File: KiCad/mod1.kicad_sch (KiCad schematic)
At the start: 67 parts, among them M1 Fan_4pin, M2 Fan_4pin, U1 W25Q128JVS

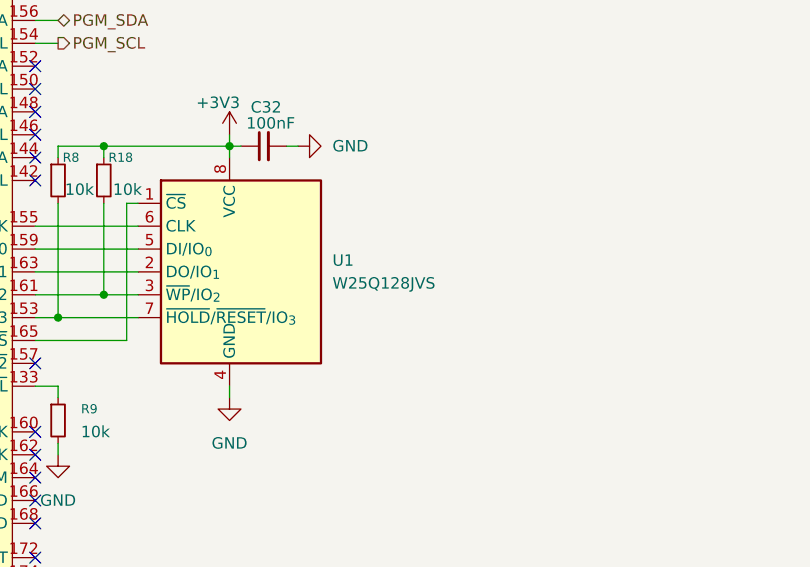
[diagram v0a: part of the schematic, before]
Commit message: Add TVS diodes for ESD protection
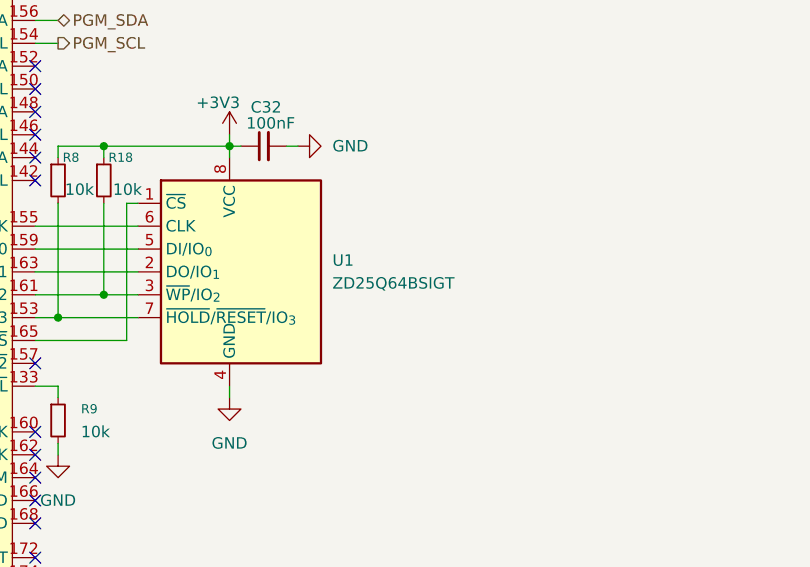
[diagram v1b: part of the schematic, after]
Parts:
- U1: value W25Q128JVS -> ZD25Q64BSIGT
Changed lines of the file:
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@@
 			)
 		)
-		(property "Value" "W25Q128JVS"
+		(property "Value" "ZD25Q64BSIGT"
 			(at 358.14 264.1599 0)
 			(effects

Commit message: Add more footprints
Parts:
- A1: footprint Module_LattePanda:LattePanda_Module_H8.0mm_Horizontal -> 124B-150A02:ATTEND_124B-150A02
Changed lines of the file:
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@@
 			)
 		)
-		(property "Footprint" "Module_LattePanda:LattePanda_Module_H8.0mm_Horizontal"
+		(property "Footprint" "124B-150A02:ATTEND_124B-150A02"
 			(at 284.48 199.39 0)
 			(effects

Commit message: Add more footprints
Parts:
- C1, C10, C11, C12, C13, C14, C15, C16, C17, C18, C19, C2, C20, C21, C22, C23, C24, C25, C26, C27, C28, C29, C3, C30, C31, C32, C33, C4, C5, C6, C7, C8, C9: footprint (none) -> Capacitor_SMD:C_0603_1608Metric
- D1: footprint (none) -> LED_SMD:LED_0805_2012Metric
- D3, D4: footprint (none) -> Diode_SMD:D_SOD-123
- M1, M2: footprint (none) -> Connector:FanPinHeader_1x04_P2.54mm_Vertical
- R1, R7: footprint (none) -> Resistor_SMD:R_0805_2012Metric
- R19, R23, R24: value 21.5k -> 22k; footprint (none) -> Resistor_SMD:R_0603_1608Metric
- R2, R20, R22, R25, R26, R3, R4, R5, R6: footprint (none) -> Resistor_SMD:R_0603_1608Metric

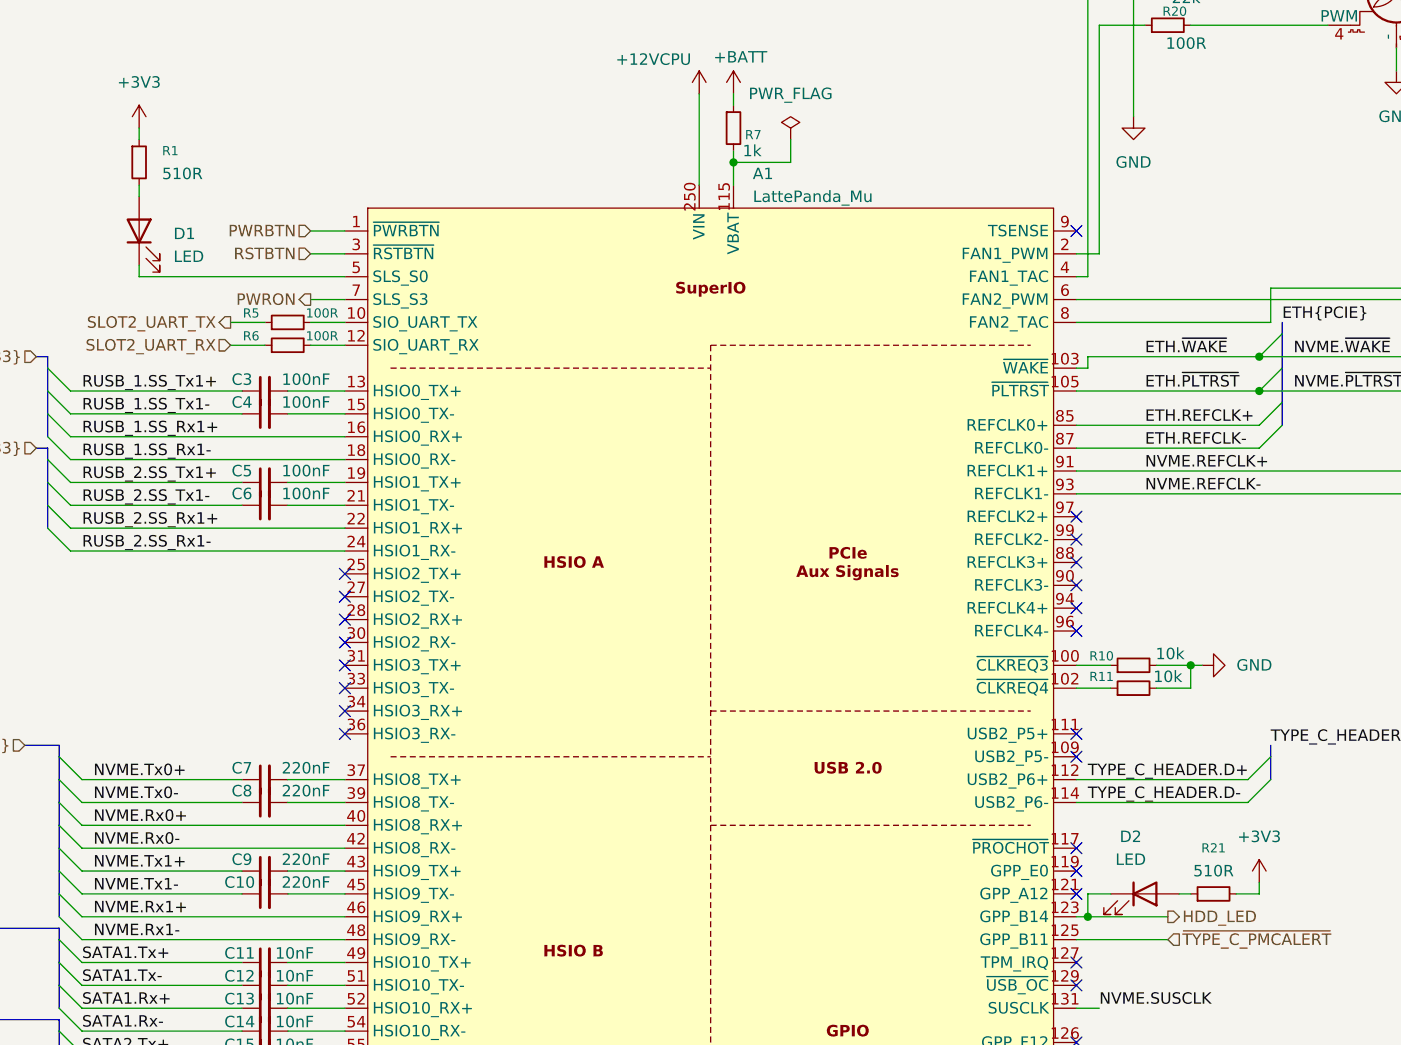
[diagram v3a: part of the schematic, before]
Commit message: Lots of tiny capacitors
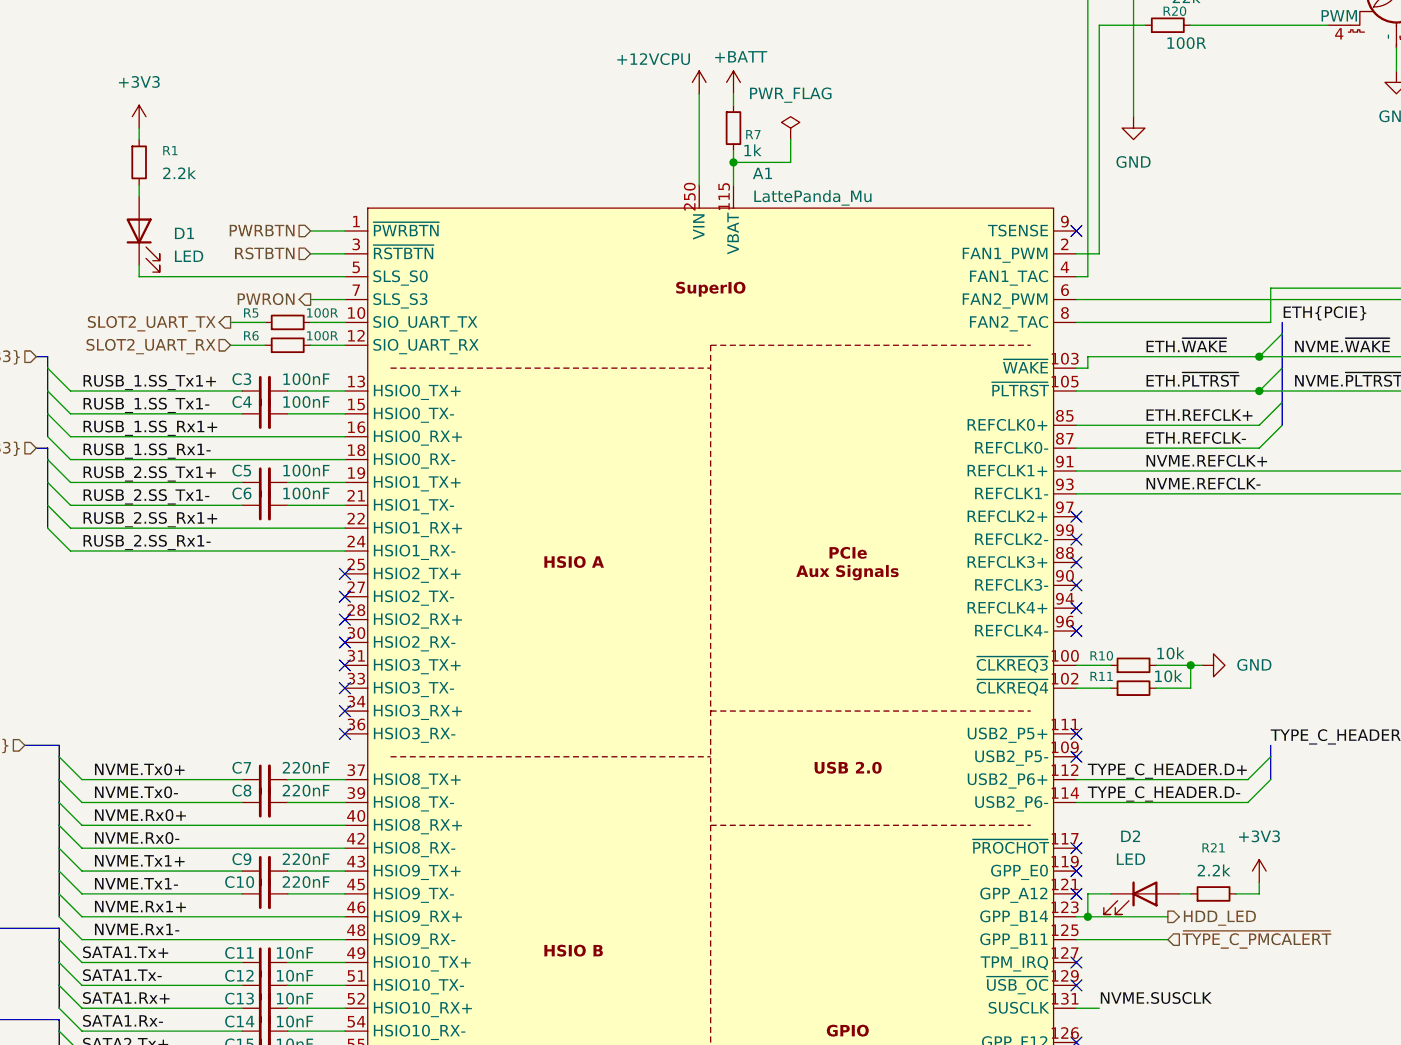
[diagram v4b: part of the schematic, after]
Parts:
- C1, C10, C11, C12, C13, C14, C15, C16, C17, C18, C19, C2, C20, C21, C22, C23, C24, C25, C26, C27, C28, C29, C3, C30, C31, C32, C33, C4, C5, C6, C7, C8, C9: footprint Capacitor_SMD:C_0603_1608Metric -> Capacitor_SMD:C_0402_1005Metric
- R1: value 510R -> 2.2k; footprint Resistor_SMD:R_0805_2012Metric -> Resistor_SMD:R_0402_1005Metric
- R10, R11, R12, R13, R14, R15, R16, R17, R18, R8: footprint (none) -> Resistor_SMD:R_0402_1005Metric
- R19, R2, R20, R22, R23, R24, R25, R26, R3, R4, R5, R6: footprint Resistor_SMD:R_0603_1608Metric -> Resistor_SMD:R_0402_1005Metric
- R21: value 510R -> 2.2k; footprint (none) -> Resistor_SMD:R_0402_1005Metric
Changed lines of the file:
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@@
 			)
 		)
-		(property "Footprint" "Capacitor_SMD:C_0603_1608Metric"
+		(property "Footprint" "Capacitor_SMD:C_0402_1005Metric"
 			(at 234.95 334.01 0)
 			(effects
@@
 			)
 		)
-		(property "Footprint" "Resistor_SMD:R_0603_1608Metric"
+		(property "Footprint" "Resistor_SMD:R_0402_1005Metric"
 			(at 237.49 92.71 0)
 			(effects
@@
 			)
 		)
-		(property "Footprint" "Capacitor_SMD:C_0603_1608Metric"
+		(property "Footprint" "Capacitor_SMD:C_0402_1005Metric"
 			(at 234.95 166.37 0)
 			(effects
@@
 			)
 		)
-		(property "Footprint" ""
+		(property "Footprint" "Resistor_SMD:R_0402_1005Metric"
 			(at 331.47 204.47 0)
 			(effects
@@
 			)
 		)
-		(property "Footprint" ""
+		(property "Footprint" "Resistor_SMD:R_0402_1005Metric"
 			(at 331.47 196.85 0)
 			(effects
@@
 			)
 		)
-		(property "Footprint" "Resistor_SMD:R_0603_1608Metric"
+		(property "Footprint" "Resistor_SMD:R_0402_1005Metric"
 			(at 335.28 57.15 0)
 			(effects
@@
 			)
 		)
-		(property "Footprint" "Capacitor_SMD:C_0603_1608Metric"
+		(property "Footprint" "Capacitor_SMD:C_0402_1005Metric"
 			(at 234.95 97.79 0)
 			(effects
@@
 			)
 		)
-		(property "Footprint" "Capacitor_SMD:C_0603_1608Metric"
+		(property "Footprint" "Capacitor_SMD:C_0402_1005Metric"
 			(at 234.95 323.85 0)
 			(effects
@@
 			)
 		)
-		(property "Footprint" "Capacitor_SMD:C_0603_1608Metric"
+		(property "Footprint" "Capacitor_SMD:C_0402_1005Metric"
 			(at 234.95 107.95 0)
 			(effects
@@
 			)
 		)
-		(property "Footprint" ""
+		(property "Footprint" "Resistor_SMD:R_0402_1005Metric"
 			(at 331.47 199.39 0)
 			(effects
@@
 			)
 		)
-		(property "Footprint" "Capacitor_SMD:C_0603_1608Metric"
+		(property "Footprint" "Capacitor_SMD:C_0402_1005Metric"
 			(at 234.95 100.33 0)
 			(effects
@@
 			)
 		)
-		(property "Footprint" "Capacitor_SMD:C_0603_1608Metric"
+		(property "Footprint" "Capacitor_SMD:C_0402_1005Metric"
 			(at 234.95 151.13 0)
 			(effects
@@
 			)
 		)
-		(property "Footprint" "Capacitor_SMD:C_0603_1608Metric"
+		(property "Footprint" "Capacitor_SMD:C_0402_1005Metric"
 			(at 234.95 173.99 0)
 			(effects
@@
 			)
 		)
-		(property "Footprint" "Capacitor_SMD:C_0603_1608Metric"
+		(property "Footprint" "Capacitor_SMD:C_0402_1005Metric"
 			(at 234.95 143.51 0)
 			(effects
@@
 			)
 		)
-		(property "Value" "510R"
+		(property "Value" "2.2k"
 			(at 340.36 151.13 90)
 			(effects
@@
 			)
 		)
-		(property "Footprint" ""
+		(property "Footprint" "Resistor_SMD:R_0402_1005Metric"
 			(at 340.36 153.67 0)
 			(effects
@@
 			)
 		)
-		(property "Footprint" "Capacitor_SMD:C_0603_1608Metric"
+		(property "Footprint" "Capacitor_SMD:C_0402_1005Metric"
 			(at 234.95 161.29 0)
 			(effects
@@
 			)
 		)
-		(property "Footprint" "Resistor_SMD:R_0603_1608Metric"
+		(property "Footprint" "Resistor_SMD:R_0402_1005Metric"
 			(at 237.49 90.17 0)
 			(effects
@@
 			)
 		)
-		(property "Footprint" ""
+		(property "Footprint" "Resistor_SMD:R_0402_1005Metric"
 			(at 331.47 130.81 0)
 			(effects
@@
 			)
 		)
-		(property "Footprint" "Capacitor_SMD:C_0603_1608Metric"
+		(property "Footprint" "Capacitor_SMD:C_0402_1005Metric"
 			(at 234.95 326.39 0)
 			(effects
@@
 			)
 		)
-		(property "Footprint" ""
+		(property "Footprint" "Resistor_SMD:R_0402_1005Metric"
 			(at 331.47 207.01 0)
 			(effects
@@
 			)
 		)
-		(property "Footprint" "Capacitor_SMD:C_0603_1608Metric"
+		(property "Footprint" "Capacitor_SMD:C_0402_1005Metric"
 			(at 234.95 331.47 0)
 			(effects
@@
 			)
 		)
-		(property "Footprint" "Capacitor_SMD:C_0603_1608Metric"
+		(property "Footprint" "Capacitor_SMD:C_0402_1005Metric"
 			(at 234.95 313.69 0)
 			(effects
@@
 			)
 		)
-		(property "Footprint" "Capacitor_SMD:C_0603_1608Metric"
+		(property "Footprint" "Capacitor_SMD:C_0402_1005Metric"
 			(at 234.95 140.97 0)
 			(effects
@@
 			)
 		)
-		(property "Footprint" "Capacitor_SMD:C_0603_1608Metric"
+		(property "Footprint" "Capacitor_SMD:C_0402_1005Metric"
 			(at 234.95 316.23 0)
 			(effects
@@
 			)
 		)
-		(property "Footprint" "Capacitor_SMD:C_0603_1608Metric"
+		(property "Footprint" "Capacitor_SMD:C_0402_1005Metric"
 			(at 234.95 184.15 0)
 			(effects
@@
 			)
 		)
-		(property "Footprint" "Capacitor_SMD:C_0603_1608Metric"
+		(property "Footprint" "Capacitor_SMD:C_0402_1005Metric"
 			(at 222.25 307.34 0)
 			(effects
@@
 			)
 		)
-		(property "Footprint" "Resistor_SMD:R_0603_1608Metric"
+		(property "Footprint" "Resistor_SMD:R_0402_1005Metric"
 			(at 389.89 52.07 0)
 			(effects
@@
 			)
 		)
-		(property "Footprint" "Resistor_SMD:R_0603_1608Metric"
+		(property "Footprint" "Resistor_SMD:R_0402_1005Metric"
 			(at 233.68 307.34 0)
 			(effects
@@
 			)
 		)
-		(property "Footprint" "Capacitor_SMD:C_0603_1608Metric"
+		(property "Footprint" "Capacitor_SMD:C_0402_1005Metric"
 			(at 234.95 163.83 0)
 			(effects
@@
 			)
 		)
-		(property "Footprint" "Capacitor_SMD:C_0603_1608Metric"
+		(property "Footprint" "Capacitor_SMD:C_0402_1005Metric"
 			(at 234.95 318.77 0)
 			(effects
@@
 			)
 		)
-		(property "Footprint" "Capacitor_SMD:C_0603_1608Metric"
+		(property "Footprint" "Capacitor_SMD:C_0402_1005Metric"
 			(at 234.95 171.45 0)
 			(effects
@@
 			)
 		)
-		(property "Footprint" "Capacitor_SMD:C_0603_1608Metric"
+		(property "Footprint" "Capacitor_SMD:C_0402_1005Metric"
 			(at 234.95 179.07 0)
 			(effects
@@
 			)
 		)
-		(property "Footprint" "Capacitor_SMD:C_0603_1608Metric"
+		(property "Footprint" "Capacitor_SMD:C_0402_1005Metric"
 			(at 222.25 309.88 0)
 			(effects
@@
 			)
 		)
-		(property "Footprint" "Resistor_SMD:R_0603_1608Metric"
+		(property "Footprint" "Resistor_SMD:R_0402_1005Metric"
 			(at 389.89 57.15 0)
 			(effects
@@
 			)
 		)
-		(property "Footprint" "Capacitor_SMD:C_0603_1608Metric"
+		(property "Footprint" "Capacitor_SMD:C_0402_1005Metric"
 			(at 234.95 186.69 0)
 			(effects
@@
 			)
 		)
-		(property "Footprint" ""
+		(property "Footprint" "Resistor_SMD:R_0402_1005Metric"
 			(at 327.66 252.73 0)
 			(effects
@@
 			)
 		)
-		(property "Footprint" "Capacitor_SMD:C_0603_1608Metric"
+		(property "Footprint" "Capacitor_SMD:C_0402_1005Metric"
 			(at 382.27 46.99 0)
 			(effects
@@
 			)
 		)
-		(property "Footprint" "Capacitor_SMD:C_0603_1608Metric"
+		(property "Footprint" "Capacitor_SMD:C_0402_1005Metric"
 			(at 234.95 168.91 0)
 			(effects
@@
 			)
 		)
-		(property "Footprint" "Resistor_SMD:R_0603_1608Metric"
+		(property "Footprint" "Resistor_SMD:R_0402_1005Metric"
 			(at 349.25 46.99 0)
 			(effects
@@
 			)
 		)
-		(property "Footprint" "Capacitor_SMD:C_0603_1608Metric"
+		(property "Footprint" "Capacitor_SMD:C_0402_1005Metric"
 			(at 234.95 336.55 0)
 			(effects
@@
 			)
 		)
-		(property "Value" "510R"
+		(property "Value" "2.2k"
 			(at 223.52 73.6599 0)
 			(effects
@@
 			)
 		)
-		(property "Footprint" "Resistor_SMD:R_0805_2012Metric"
+		(property "Footprint" "Resistor_SMD:R_0402_1005Metric"
 			(at 220.98 72.39 0)
 			(effects
@@
 			)
 		)
-		(property "Footprint" ""
+		(property "Footprint" "Resistor_SMD:R_0402_1005Metric"
 			(at 332.74 252.73 0)
 			(effects
@@
 			)
 		)
-		(property "Footprint" "Resistor_SMD:R_0603_1608Metric"
+		(property "Footprint" "Resistor_SMD:R_0402_1005Metric"
 			(at 403.86 46.99 0)
 			(effects
@@
 			)
 		)
-		(property "Footprint" "Capacitor_SMD:C_0603_1608Metric"
+		(property "Footprint" "Capacitor_SMD:C_0402_1005Metric"
 			(at 331.47 46.99 0)
 			(effects
@@
 			)
 		)
-		(property "Footprint" "Capacitor_SMD:C_0603_1608Metric"
+		(property "Footprint" "Capacitor_SMD:C_0402_1005Metric"
 			(at 234.95 328.93 0)
 			(effects
@@
 			)
 		)
-		(property "Footprint" "Resistor_SMD:R_0603_1608Metric"
+		(property "Footprint" "Resistor_SMD:R_0402_1005Metric"
 			(at 233.68 309.88 0)
 			(effects
@@
 			)
 		)
-		(property "Footprint" "Resistor_SMD:R_0603_1608Metric"
+		(property "Footprint" "Resistor_SMD:R_0402_1005Metric"
 			(at 386.08 62.23 0)
 			(effects
@@
 			)
 		)
-		(property "Footprint" ""
+		(property "Footprint" "Resistor_SMD:R_0402_1005Metric"
 			(at 331.47 209.55 0)
 			(effects
@@
 			)
 		)
-		(property "Footprint" "Capacitor_SMD:C_0603_1608Metric"
+		(property "Footprint" "Capacitor_SMD:C_0402_1005Metric"
 			(at 234.95 110.49 0)
 			(effects
@@
 			)
 		)
-		(property "Footprint" "Capacitor_SMD:C_0603_1608Metric"
+		(property "Footprint" "Capacitor_SMD:C_0402_1005Metric"
 			(at 234.95 176.53 0)
 			(effects
@@
 			)
 		)
-		(property "Footprint" "Resistor_SMD:R_0603_1608Metric"
+		(property "Footprint" "Resistor_SMD:R_0402_1005Metric"
 			(at 234.95 265.43 0)
 			(effects
@@
 			)
 		)
-		(property "Footprint" ""
+		(property "Footprint" "Resistor_SMD:R_0402_1005Metric"
 			(at 331.47 128.27 0)
 			(effects
@@
 			)
 		)
-		(property "Footprint" "Capacitor_SMD:C_0603_1608Metric"
+		(property "Footprint" "Capacitor_SMD:C_0402_1005Metric"
 			(at 350.52 248.92 0)
 			(effects
@@
 			)
 		)
-		(property "Footprint" "Resistor_SMD:R_0603_1608Metric"
+		(property "Footprint" "Resistor_SMD:R_0402_1005Metric"
 			(at 335.28 52.07 0)
 			(effects
@@
 			)
 		)
-		(property "Footprint" ""
+		(property "Footprint" "Resistor_SMD:R_0402_1005Metric"
 			(at 331.47 201.93 0)
 			(effects
@@
 			)
 		)
-		(property "Footprint" "Capacitor_SMD:C_0603_1608Metric"
+		(property "Footprint" "Capacitor_SMD:C_0402_1005Metric"
 			(at 234.95 153.67 0)
 			(effects
@@
 			)
 		)
-		(property "Footprint" "Capacitor_SMD:C_0603_1608Metric"
+		(property "Footprint" "Capacitor_SMD:C_0402_1005Metric"
 			(at 234.95 321.31 0)
 			(effects

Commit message: Add most passive component footprints
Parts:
- D1: footprint LED_SMD:LED_0805_2012Metric -> LED_SMD:LED_0603_1608Metric
- D2: footprint (none) -> LED_SMD:LED_0603_1608Metric
- R9: footprint (none) -> Resistor_SMD:R_0402_1005Metric
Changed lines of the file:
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@@
 			)
 		)
-		(property "Footprint" ""
+		(property "Footprint" "LED_SMD:LED_0603_1608Metric"
 			(at 332.74 153.67 0)
 			(effects
@@
 			)
 		)
-		(property "Footprint" ""
+		(property "Footprint" "Resistor_SMD:R_0402_1005Metric"
 			(at 327.66 279.4 0)
 			(effects
@@
 			)
 		)
-		(property "Footprint" "LED_SMD:LED_0805_2012Metric"
+		(property "Footprint" "LED_SMD:LED_0603_1608Metric"
 			(at 220.98 80.01 0)
 			(effects
